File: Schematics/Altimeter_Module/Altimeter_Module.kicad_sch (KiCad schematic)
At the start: 112 parts, among them J1 Stack Male Edge Connector, J2 Main E-Match, J3 Drogue E-Match, J4 USB_C_Female_USB2_Small, J5 SWD_01x04_Pin, Q1 AO3400A, Q2 AO4406AL, Q3 AO3400A, Q4 AO3400A, Q5 AO4406AL, SW1 SW_STM_RESET, SW2 SW_STM_BOOT_MODE, U1 KX134-1211, U10 ACS70331EOLC, U11 CP2102N-Axx-xQFN28, U12 AMS1117-3.3, U2 MS560702BA03-50, U3 W25Q128JVS, U4 LM66100DCKR, U5 LM66100DCKR, U6 STM32F103CBT6, U7 LM66100DCKR, U8 ISO1042BDWVR, U9 MPU-6050, Y1 X322516MMB4SI

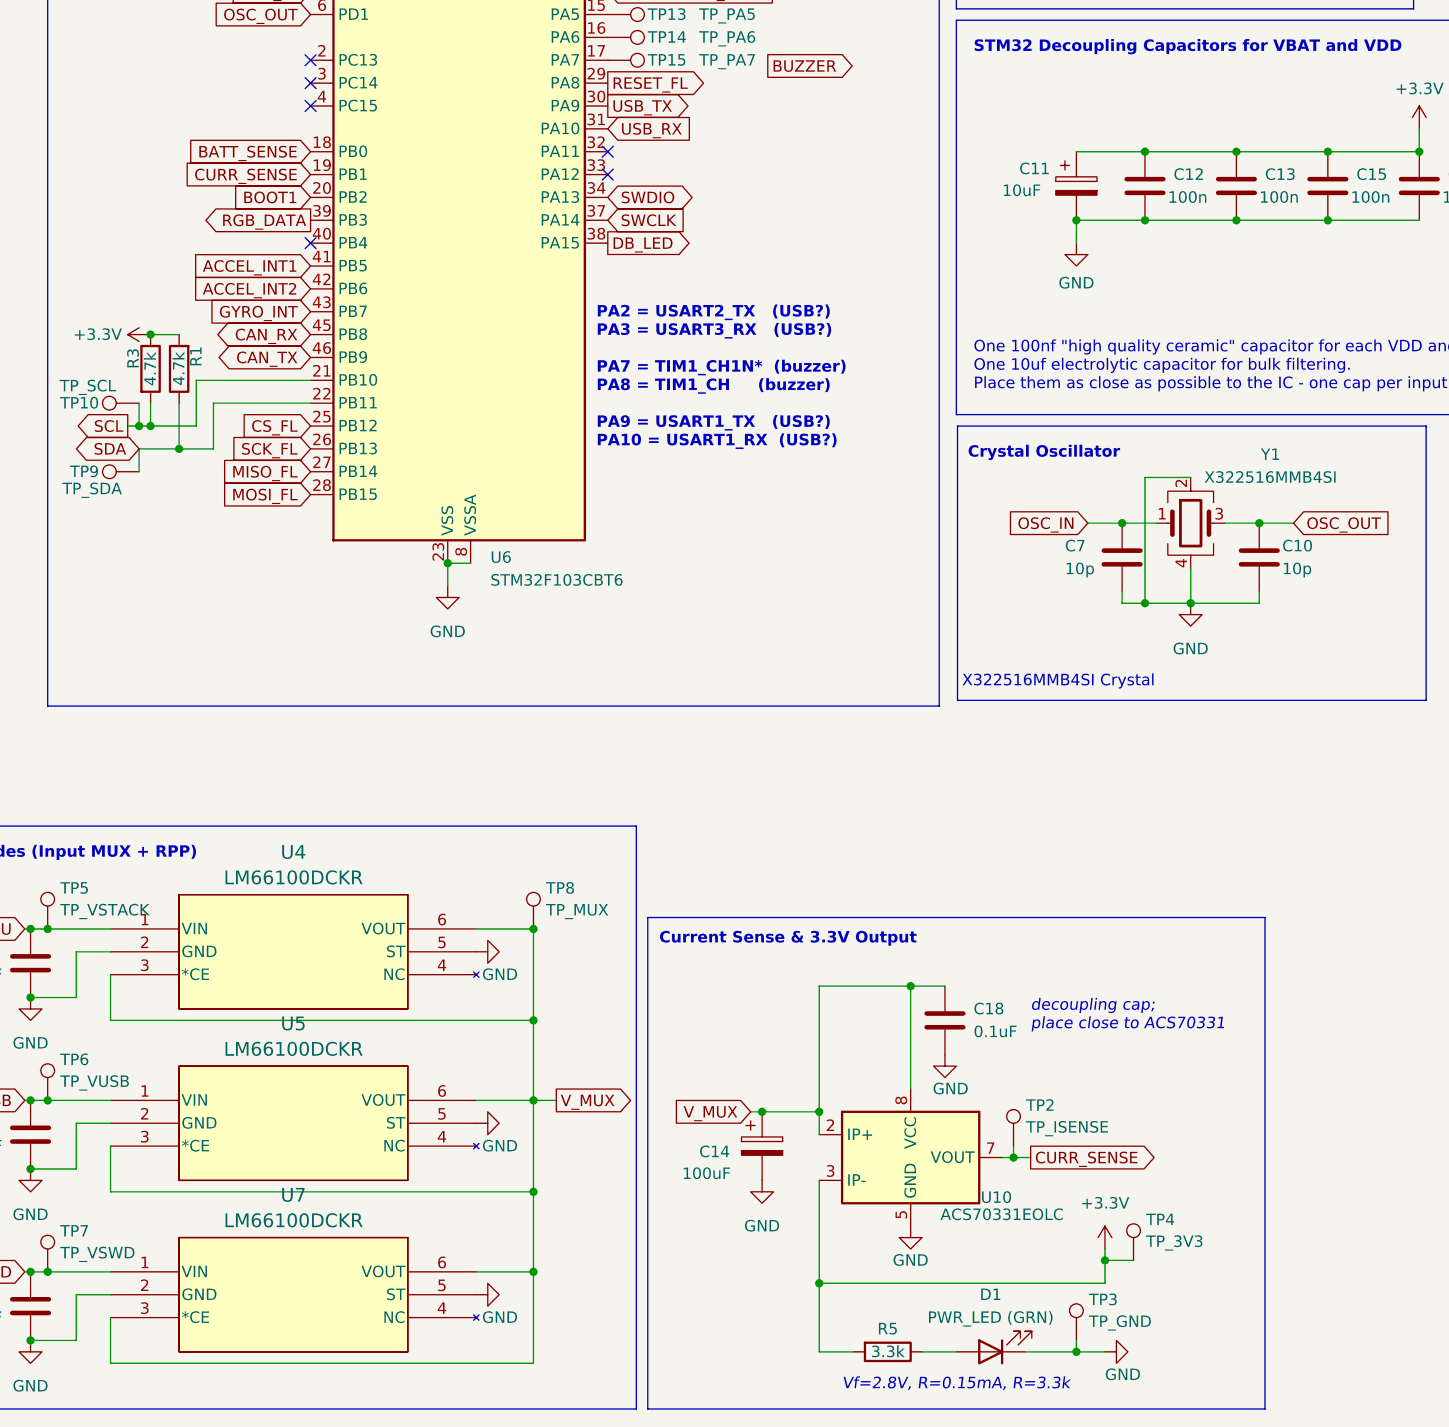
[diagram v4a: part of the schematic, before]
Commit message: Removed ACS70331 current sensor
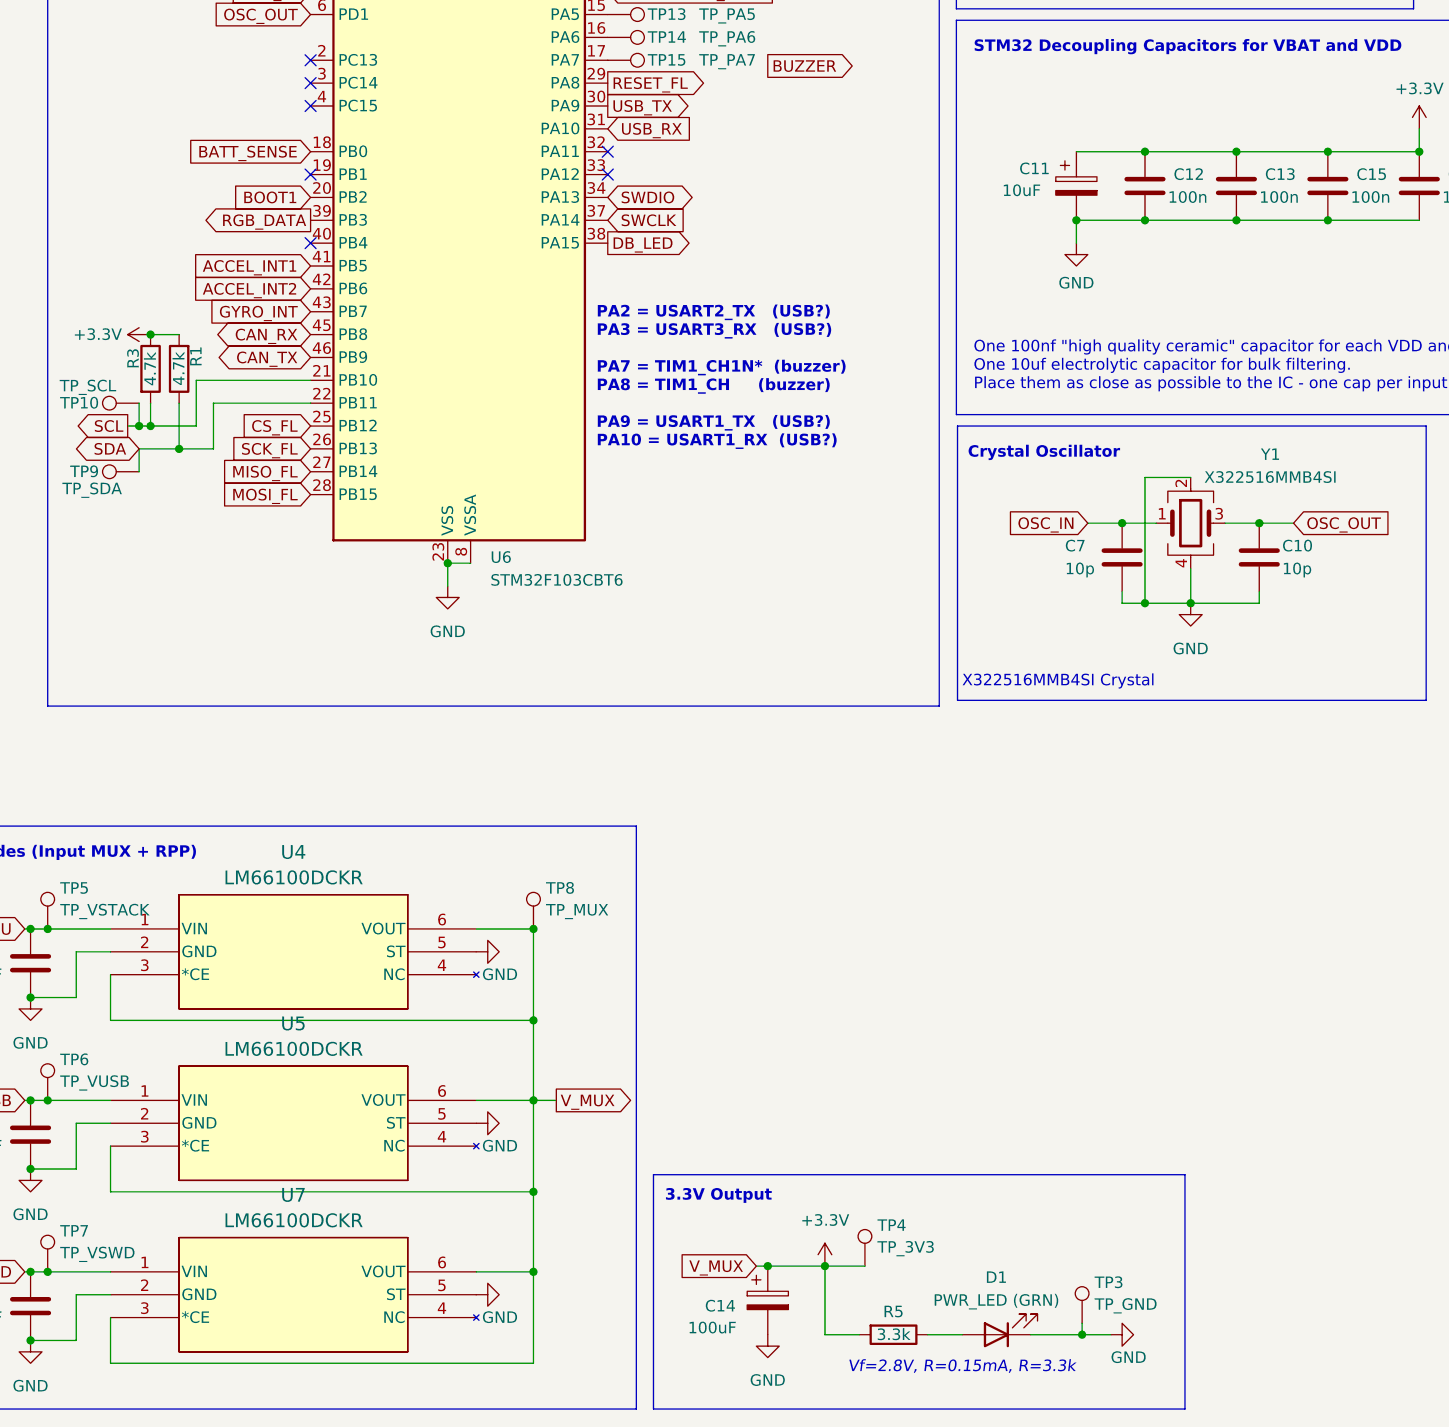
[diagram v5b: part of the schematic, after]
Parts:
- removed C18: 0.1uF, Capacitor_SMD:C_0603_1608Metric, symbol Device:C
- removed TP2: TP_ISENSE, TestPoint:TestPoint_Pad_1.5x1.5mm, symbol Connector:TestPoint
- removed U10: ACS70331EOLC, footprints:SOIC127P600X175-8N, symbol Sensor_Current:ACS706xLC-05C
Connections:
- net V_MUX is gone; now on net +3.3V: C14.1, TP8.1, U4.3 (*CE), U4.6 (VOUT), U5.3 (*CE), U5.6 (VOUT), U7.3 (*CE), U7.6 (VOUT)
- net CURR_SENSE: no longer names the net of U6.19 (PB1)
- no-connect marks 36 -> 37
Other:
- note added: "3.3V Output"
- note removed: "Current Sense & 3.3V Output"
- note removed: "decoupling cap; place close to ACS70331"
- moved on the sheet: C14, D1, R5, TP3, TP4

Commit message: Adjusted schematic documentation
Noted that battery sense circuit will remain for redundancy, and that QMA6100P accelerometer was used in place of KX134
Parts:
- U1: value KX134-1211 -> QMA6100P; LCSC C2157908 -> C2887190
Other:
- note added: "I2C ADDRESS: 0x12 (ADDR 0.0V) >0x13 (ADDR 3.3V)"
- note added: "NOTE: Due to supply shortages during manufacturing, we made a last-minute change from the KX134-1211 (LCSC C2157908) to the pin-compatible QMA6100P (LCSC C2887190). See the table for a comparison between the two parts."
- note added: "OLD KX134 I2C ADDRESS: 0x1E (ADDR 0.0V) >0x1F (ADDR 3.3V)"
- note added: "Place in EXACT center of PCB"
- note added: "QMA6100P Accelerometer (I2C)"
- note added: "Redundant battery sense for safety or standalone usage (batt sense already handled by power module)"
- note added: "Stack Edge Connector [RUNNING ON B-RAILS]"
- note removed: "I2C ADDRESS: 0x1E (ADDR 0.0V) >0x1F (ADDR 3.3V)"
- note removed: "KX134 Accelerometer (I2C)"
- note removed: "NEW I2C ADDRESS: 0x12 (ADDR 0.0V) >0x13 (ADDR 3.3V)"
- note removed: "NOTE: Due to supply shortages during manufacturing, we made the last-minute change to the pin-compatible QMA6100P (LCSC C2887190). See the table for a comparison between the two parts."
- note removed: "Place in center of PCB"
- note removed: "Stack Edge Connector [SECONDARY MODULE]"
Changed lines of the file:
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@@
     (effects (font (size 1.27 1.27) (thickness 0.254) bold) (justify left bottom))
   )
-  (text "Stack Edge Connector [SECONDARY MODULE]" (at 349.25 63.5 0)
+  (text "Stack Edge Connector [RUNNING ON B-RAILS]" (at 349.25 63.5 0)
     (effects (font (size 1.27 1.27) (thickness 0.254) bold) (justify left bottom))
   )
-  (text "NOTE: Due to supply shortages during\nmanufacturing, we made the last-minute\nchange to the pin-compatible QMA6100P\n(LCSC C2887190). See the table for a\ncomparison between the two parts."
-    (at 50.165 245.745 0)
+  (text "NOTE: Due to supply shortages during\nmanufacturing, we made a last-minute\nchange from the KX134-1211\n(LCSC C2157908) to the pin-compatible\nQMA6100P (LCSC C2887190). See the\ntable for a comparison between the\ntwo parts."
+    (at 50.165 249.555 0)
     (effects (font (size 1.27 1.27)) (justify left bottom))
   )
@@
     (effects (font (size 1.27 1.27) (thickness 0.254) bold) (justify left bottom))
   )
-  (text "I2C ADDRESS:\n0x1E (ADDR 0.0V)\n>0x1F (ADDR 3.3V)" (at 90.805 203.835 0)
+  (text "I2C ADDRESS:\n0x12 (ADDR 0.0V)\n>0x13 (ADDR 3.3V)" (at 90.805 203.835 0)
     (effects (font (size 1.27 1.27)) (justify right bottom))
   )
@@
     (effects (font (size 1.27 1.27) (thickness 0.254) bold) (justify left bottom))
   )
-  (text "Place in center of PCB" (at 67.945 231.775 0)
+  (text "Place in EXACT center of PCB" (at 60.96 231.775 0)
     (effects (font (size 1.27 1.27)) (justify left bottom))
   )
@@
     (effects (font (size 1.27 1.27) (thickness 0.254) bold) (justify left bottom))
   )
-  (text "NEW I2C ADDRESS:\n0x12 (ADDR 0.0V)\n>0x13 (ADDR 3.3V)"
+  (text "OLD KX134 I2C ADDRESS:\n0x1E (ADDR 0.0V)\n>0x1F (ADDR 3.3V)"
     (at 90.17 264.16 0)
     (effects (font (size 1.27 1.27)) (justify right bottom))
@@
     (effects (font (size 1.27 1.27) (thickness 0.254) bold) (justify left bottom))
   )
-  (text "KX134 Accelerometer (I2C)" (at 13.335 200.025 0)
+  (text "QMA6100P Accelerometer (I2C)" (at 13.335 200.025 0)
     (effects (font (size 1.27 1.27) (thickness 0.254) bold) (justify left bottom))
   )
@@
     (effects (font (size 1.27 1.27) italic) (justify left bottom))
   )
+  (text "Redundant battery\nsense for safety\nor standalone usage\n(batt sense already\nhandled by power\nmodule)\n"
+    (at 398.145 83.185 0)
+    (effects (font (size 1.27 1.27)) (justify left bottom))
+  )
   (text "USB-UART Bridge" (at 354.965 153.035 0)
     (effects (font (size 1.27 1.27) (thickness 0.254) bold) (justify left bottom))
@@
       (effects (font (size 1.524 1.524)))
     )
-    (property "Value" "KX134-1211" (at 55.88 203.9426 0)
+    (property "Value" "QMA6100P" (at 55.88 203.9426 0)
       (effects (font (size 1.524 1.524)))
     )
@@
       (effects (font (size 1.27 1.27) italic) hide)
     )
-    (property "LCSC" "C2157908" (at 34.29 210.82 0)
+    (property "LCSC" "C2887190" (at 34.29 210.82 0)
       (effects (font (size 1.27 1.27)) hide)
     )

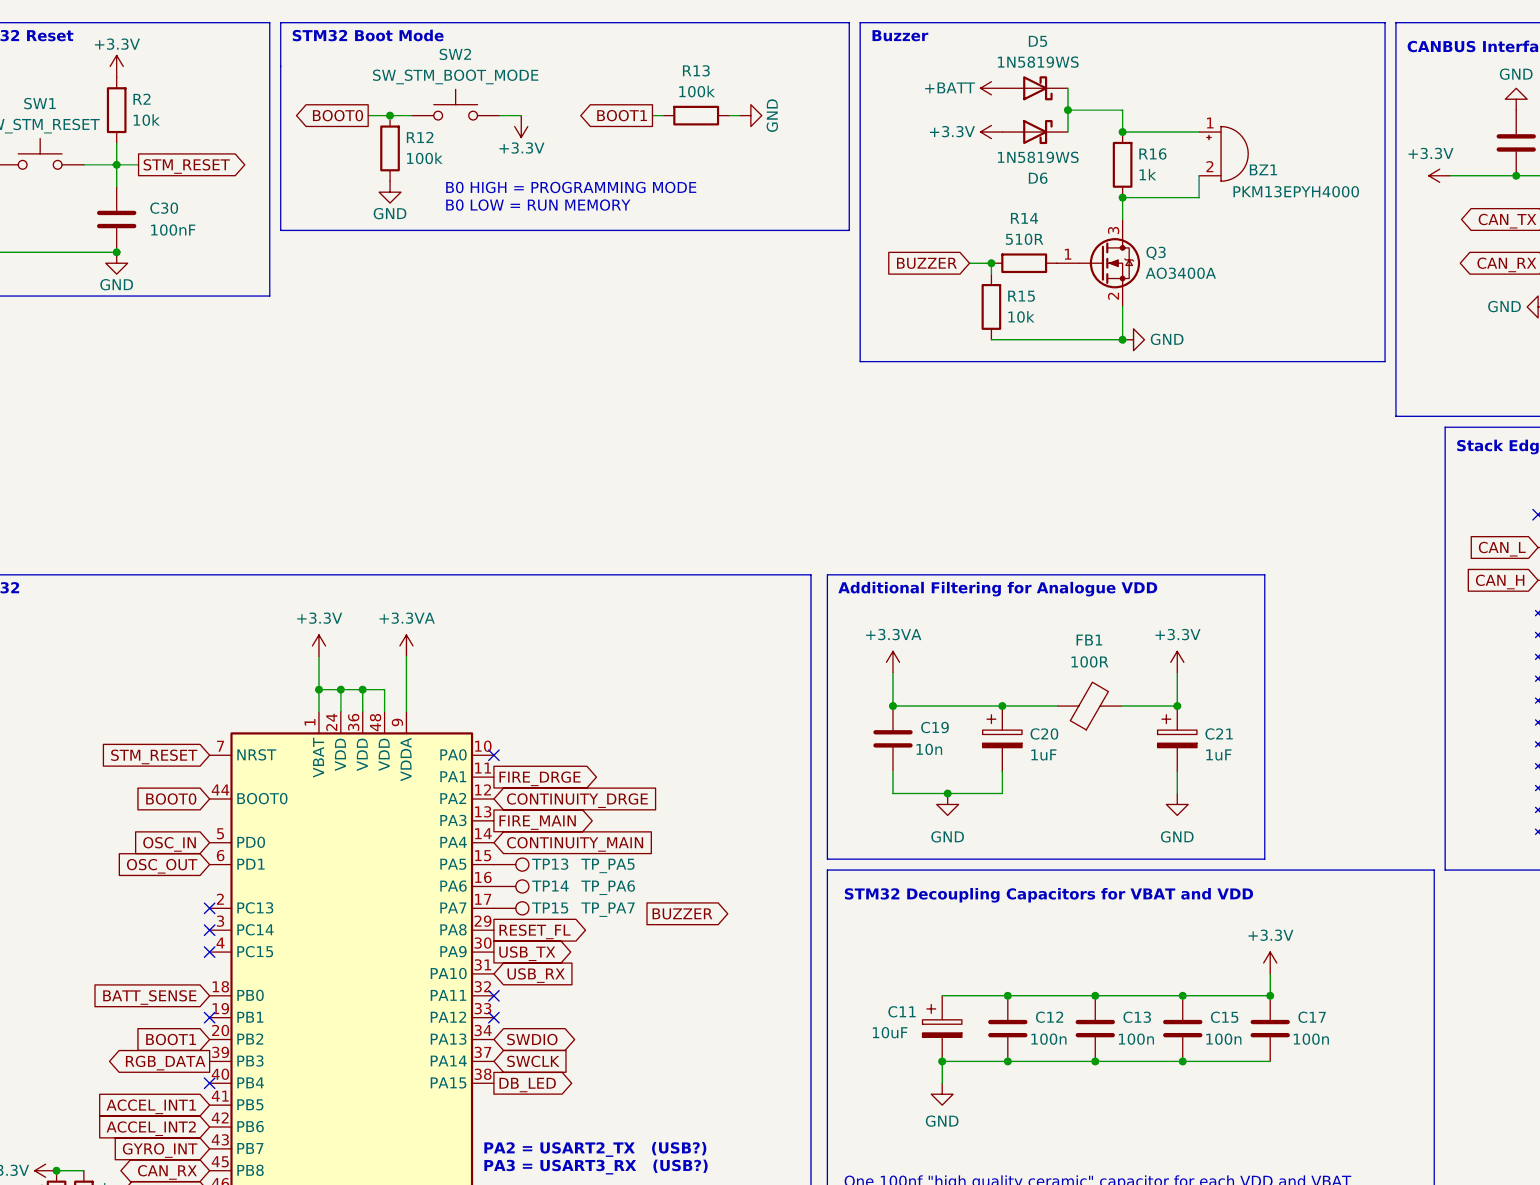
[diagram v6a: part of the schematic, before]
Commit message: Added revised buzzer driver circuit
Changed to buzzer PS1240P02BT (previous stock issues), plus switched to using 2-pin inverse PWM drive via a TPM8837C H-Bridge IC. Now Vpp should be ~14.8V.
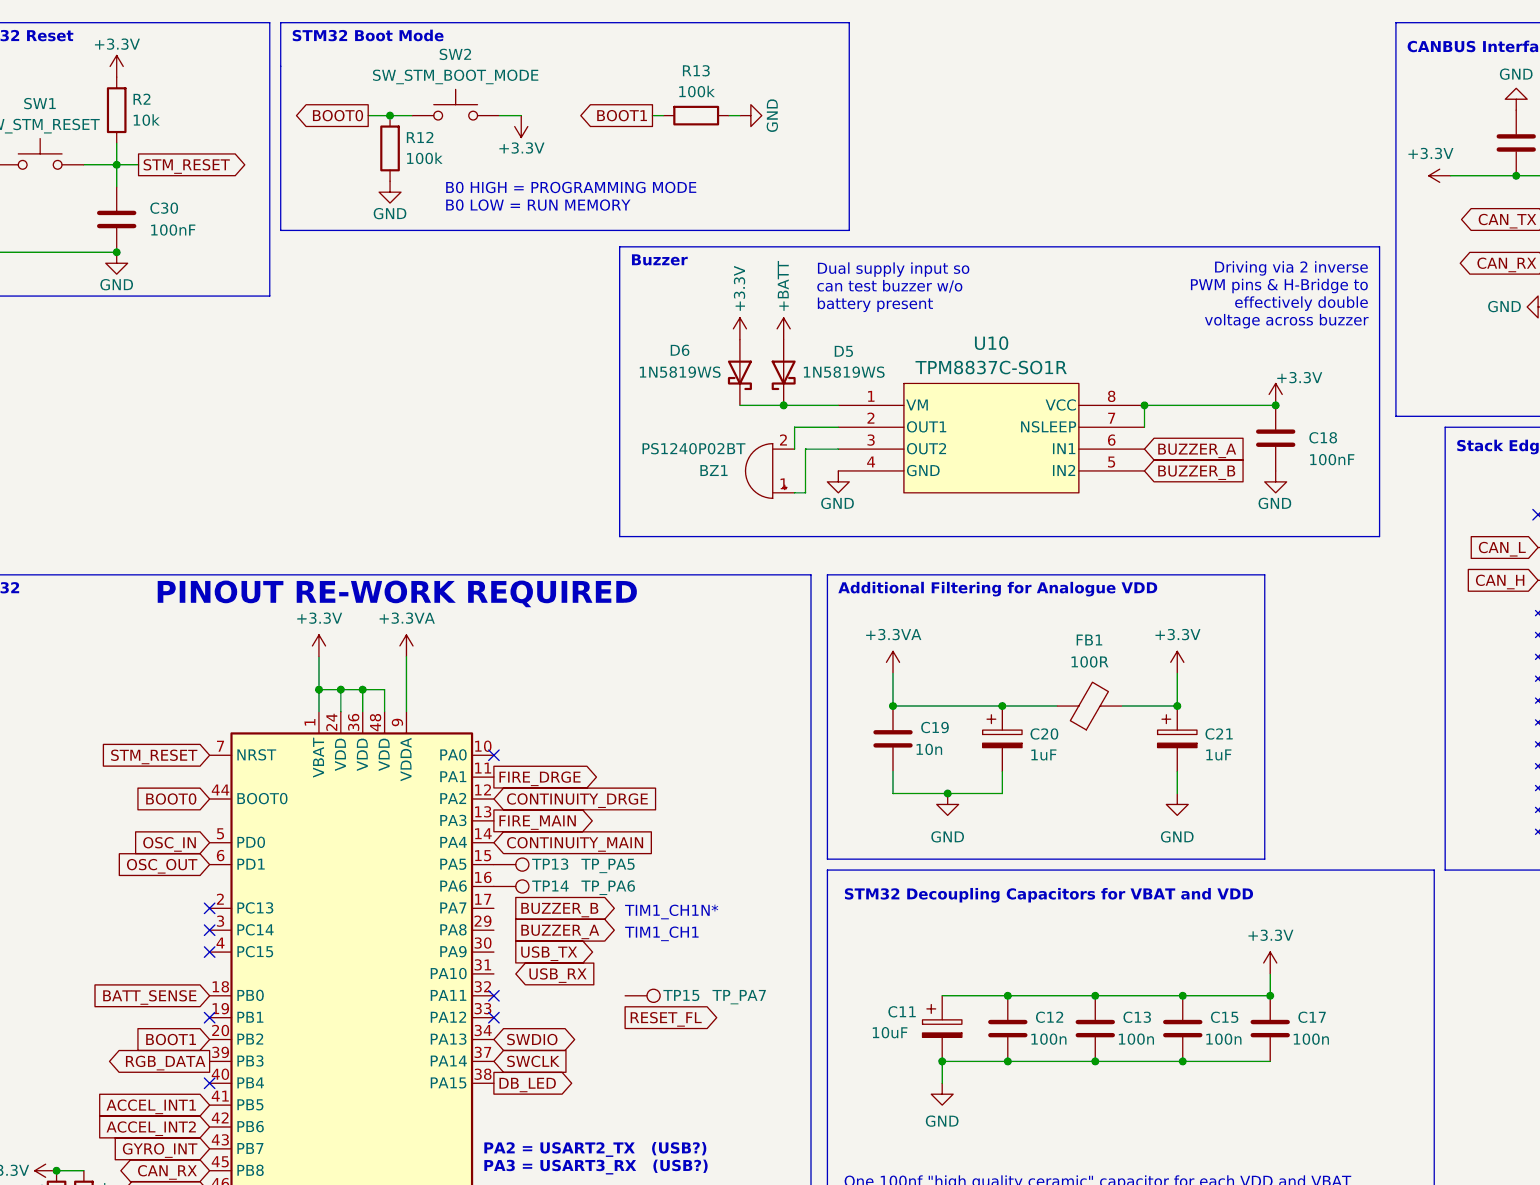
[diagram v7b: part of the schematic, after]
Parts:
- removed Q3: AO3400A, Package_TO_SOT_SMD:SOT-23, symbol Transistor_FET:AO3400A
- removed R14: 510R, Resistor_SMD:R_0603_1608Metric, symbol Device:R
- removed R15: 10k, Resistor_SMD:R_0603_1608Metric, symbol Device:R
- removed R16: 1k, Resistor_SMD:R_0603_1608Metric, symbol Device:R
- added C18: 100nF, Capacitor_SMD:C_0603_1608Metric, symbol Device:C
- added U10: TPM8837C-SO1R, footprints:SOP-8_TPK, symbol TPM8837C-SO1R:TPM8837C-SO1R
- BZ1: value PKM13EPYH4000 -> PS1240P02BT; Digikey 490-4698-1-ND -> 445-2525-1-ND
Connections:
- net +3.3V: now also C18.1, U10.7 (NSLEEP), U10.8 (VCC)
- net GND: now also C18.2, U10.4 (GND)
- net RESET_FL: no longer U6.29 (PA8)
- net USB_RX: no longer U6.31 (PA10)
- net USB_TX: no longer U6.30 (PA9)
- net at D5.1 (K), D6.1 (K): now also U10.1 (VM); no longer BZ1.1 (-)
- net at BZ1.2 (+): now also U10.2 (OUT1)
- net at U6.17 (PA7): no longer TP15.1
- new net: BZ1.1 (-), U10.3 (OUT2)
- new net BUZZER_A: U10.6 (IN1)
- new net BUZZER_B: U10.5 (IN2)
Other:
- note added: "Driving via 2 inverse PWM pins & H-Bridge to effectively double voltage across buzzer"
- note added: "Dual supply input so can test buzzer w/o battery present"
- note added: "PINOUT RE-WORK REQUIRED"
- note added: "TIM1_CH1"
- note added: "TIM1_CH1N*"
- moved on the sheet: BZ1, D5, D6, TP15
